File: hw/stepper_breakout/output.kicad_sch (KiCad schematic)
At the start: 5 parts

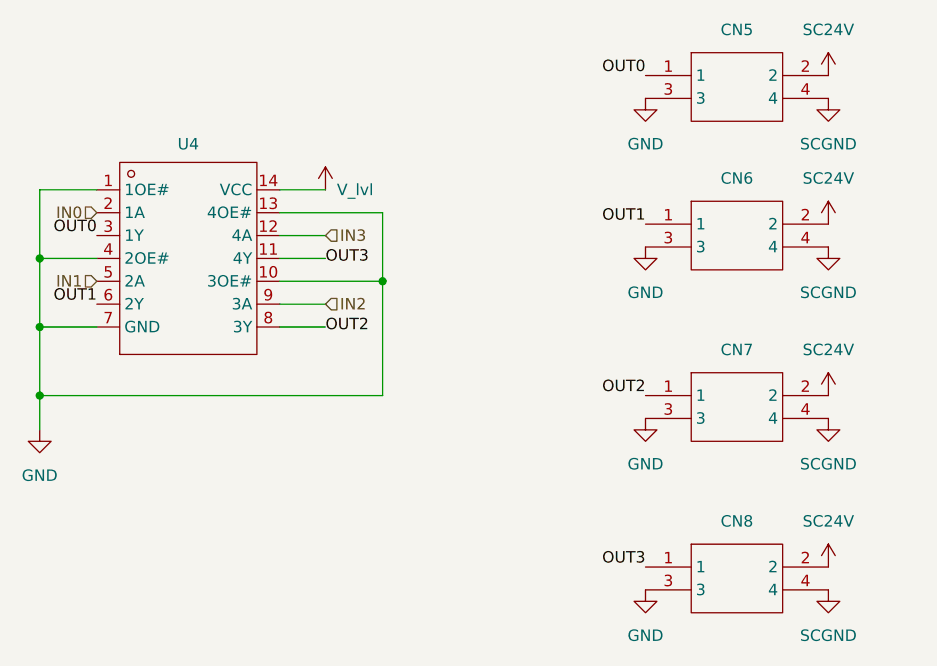
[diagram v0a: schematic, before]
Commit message: Fixed pcb connector pinout
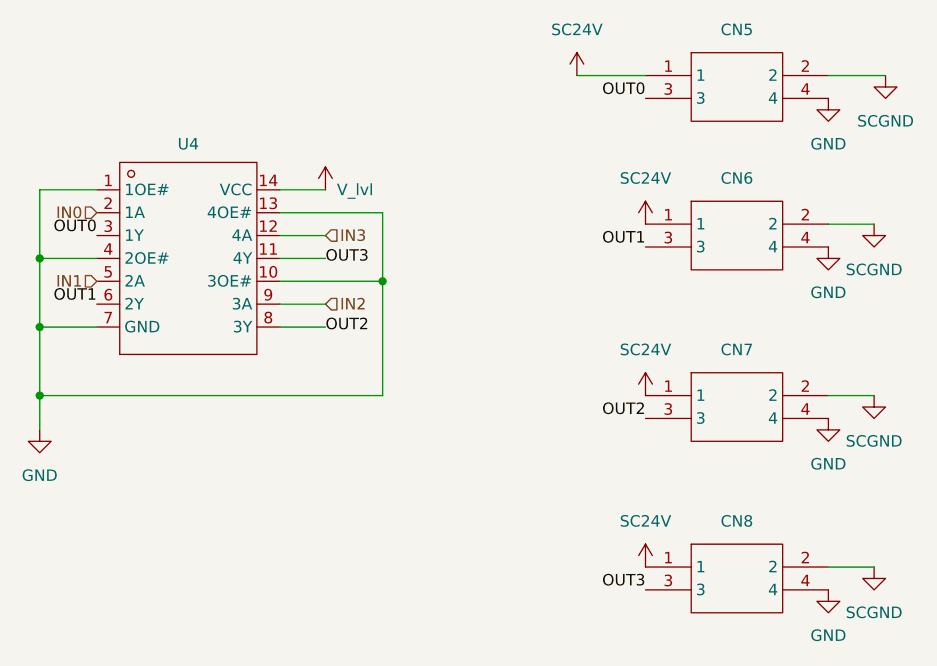
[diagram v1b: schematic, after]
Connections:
- net GND: now also CN5.4, CN6.4, CN7.4, CN8.4; no longer CN5.3, CN6.3, CN7.3, CN8.3
- net OUT0: now also CN5.3; no longer CN5.1
- net OUT1: now also CN6.3; no longer CN6.1
- net OUT2: now also CN7.3; no longer CN7.1
- net OUT3: now also CN8.3; no longer CN8.1
- net SC24V: now also CN5.1, CN6.1, CN7.1, CN8.1; no longer CN5.2, CN6.2, CN7.2, CN8.2
- net SCGND: now also CN5.2, CN6.2, CN7.2, CN8.2; no longer CN5.4, CN6.4, CN7.4, CN8.4

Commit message: Reannotated
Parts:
- U2: renamed from U4; LCSC (none) -> C155176
- renumbered CN5 to CN1, CN6 to CN2, CN7 to CN3, CN8 to CN4

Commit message: Added test mode
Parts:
- CN1, CN2, CN3, CN4: LCSC (none) -> C24697; Supplier Part C24697 -> (none)
- U2: Supplier Part C155176 -> (none)
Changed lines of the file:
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@@
 			)
 		)
-		(property "Supplier Part" "C24697"
+		(property "LCSC" "C24697"
 			(at 134.62 67.31 0)
 			(hide yes)
@@
 			)
 		)
-		(property "Supplier Part" "C155176"
+		(property "LCSC" "C155176"
 			(at 73.66 50.8 0)
 			(hide yes)
@@
 		)
 		(property "LCSC Part Name" "三态输出，四路总线缓冲门"
-			(at 73.66 50.8 0)
-			(hide yes)
-			(show_name no)
-			(do_not_autoplace no)
-			(effects
-				(font
-					(size 1.27 1.27)
-				)
-			)
-		)
-		(property "LCSC" "C155176"
 			(at 73.66 50.8 0)
 			(hide yes)
@@
 			)
 		)
-		(property "Supplier Part" "C24697"
+		(property "LCSC" "C24697"
 			(at 134.62 48.26 0)
 			(hide yes)
@@
 			)
 		)
-		(property "Supplier Part" "C24697"
+		(property "LCSC" "C24697"
 			(at 134.62 31.75 0)
 			(hide yes)
@@
 			)
 		)
-		(property "Supplier Part" "C24697"
+		(property "LCSC" "C24697"
 			(at 134.62 86.36 0)
 			(hide yes)
